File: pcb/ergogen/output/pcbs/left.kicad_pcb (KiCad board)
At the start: 2 copper layers, 143.4 x 86.2 mm, 49 parts

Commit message: Go Choc-only, add KiCad guide and case feel notes
- Drop the MX variant: one PCB per half with a Choc v1/v2 hot-swap
  footprint (center hole widened to 5.05mm for Choc v2).
- Ergogen outputs renamed to left/right PCBs and plate_left/right.
- docs/kicad-guide.md: beginner steps for finishing the PCB in KiCad.
- README: case ideas to keep a good typing feel (gasket mount,
  swappable plate materials, foam, flex cuts, weight).

Co-Authored-By: Claude Opus 5.5 <noreply@anthropic.com>
Claude-Session: https://claude.ai/code/session_017zNm7dMSTHELcztuNr6aNy
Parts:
- removed J1: , header6
- added D23: , ComboDiode, F.Cu at (95.2, -52.2)
- added D24: , ComboDiode, F.Cu at (114.3, 5.00)
- added D25: , ComboDiode, F.Cu at (104.8, -9.85)
- added ROT1: , rotary_encoder, F.Cu at (104.8, -19.1)
- added S23: , Choc_V1V2_Hotswap, F.Cu at (95.2, -57.2)
- added S24: , Choc_V1V2_Hotswap, F.Cu at (114.3, 0.00)
- S1, S10, S11, S12, S13, S14, S15, S16, S17, S18, S19, S2, S20, S21, S22, S3, S4, S5, S6, S7, S8, S9: footprint MX -> Choc_V1V2_Hotswap
- moved JST1 295.3 mm to (9.53, -9.53)
- moved D19 241.1 mm to (76.2, -33.1)
- moved D20 241.1 mm to (76.2, -52.2)
- moved D3 241.1 mm to (0.00, -33.1)
- moved D4 241.1 mm to (0.00, -52.2)
- moved D7 241.1 mm to (19.1, -33.1)
- moved D8 241.1 mm to (19.1, -52.2)
- moved S19 241.1 mm to (76.2, -38.1)
- moved S20 241.1 mm to (76.2, -57.2)
- moved S3 241.1 mm to (0.00, -38.1)
- moved S4 241.1 mm to (0.00, -57.2)
- moved S7 241.1 mm to (19.1, -38.1)
- moved S8 241.1 mm to (19.1, -57.2)
- moved D11 241.1 mm to (38.1, -33.1)
- moved D12 241.1 mm to (38.1, -52.2)
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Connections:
- net right_c10_bottom renamed left_c2_top
- net right_c10_home renamed left_c3_thumb
- net right_c10_thumb renamed left_c2_home
- net right_c10_top renamed left_c3_bottom
- net right_c11_bottom renamed left_c3_top
- net right_c11_home renamed left_c4_thumb
- net right_c11_thumb renamed left_c3_home
- net right_c11_top renamed left_c4_bottom
- net right_c12_bottom renamed left_c4_top
- net right_c12_home renamed left_c5_thumb
- net right_c12_thumb renamed left_c4_home
- net right_c12_top renamed left_c5_home
- net right_c8_bottom renamed left_c0_top
- net right_c8_home renamed left_c1_thumb
- net right_c8_thumb renamed left_c0_home
- net right_c8_top renamed left_c1_bottom
- net right_c9_bottom renamed left_c1_top
- net right_c9_home renamed left_c2_thumb
- net right_c9_thumb renamed left_c1_home
- net right_c9_top renamed left_c2_bottom
- net right_e_home renamed left_c0_thumb
- net right_e_top renamed left_c0_bottom
- D1 pad 1: ROW1 -> ROW3
- D10 pad 1: ROW0 -> ROW2
- D11 pad 1: ROW3 -> ROW1
- D12 pad 1: ROW2 -> ROW0
- D13 pad 1: ROW1 -> ROW3
- D14 pad 1: ROW0 -> ROW2
- D15 pad 1: ROW3 -> ROW1
- D16 pad 1: ROW2 -> ROW0
- D17 pad 1: ROW1 -> ROW3
- D18 pad 1: ROW0 -> ROW2
- D19 pad 1: ROW3 -> ROW1
- D2 pad 1: ROW0 -> ROW2
- D20 pad 1: ROW2 -> ROW0
- D21 pad 1: ROW1 -> ROW3
- D22 pad 1: ROW0 -> ROW1
- D3 pad 1: ROW3 -> ROW1
- D4 pad 1: ROW2 -> ROW0
- D5 pad 1: ROW1 -> ROW3
- D6 pad 1: ROW0 -> ROW2
- D7 pad 1: ROW3 -> ROW1
- D8 pad 1: ROW2 -> ROW0
- D9 pad 1: ROW1 -> ROW3
- S1 pad 1: COL7 -> COL0
- S10 pad 1: COL9 -> COL2
- S11 pad 1: COL10 -> COL2
- S12 pad 1: COL10 -> COL2
- S13 pad 1: COL10 -> COL3
- S14 pad 1: COL10 -> COL3
- S15 pad 1: COL11 -> COL3
- S16 pad 1: COL11 -> COL3
- S17 pad 1: COL11 -> COL4
- S18 pad 1: COL11 -> COL4
- S19 pad 1: COL12 -> COL4
- S2 pad 1: COL7 -> COL0
- S20 pad 1: COL12 -> COL4
- S21 pad 1: COL12 -> COL5
- S22 pad 1: COL12 -> COL5
- S3 pad 1: COL8 -> COL0
- S4 pad 1: COL8 -> COL0
- S5 pad 1: COL8 -> COL1
- S6 pad 1: COL8 -> COL1
- S7 pad 1: COL9 -> COL1
- S8 pad 1: COL9 -> COL1
- S9 pad 1: COL9 -> COL2
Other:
- board size 143.4 x 86.2 mm -> 143.3 x 86.2 mm

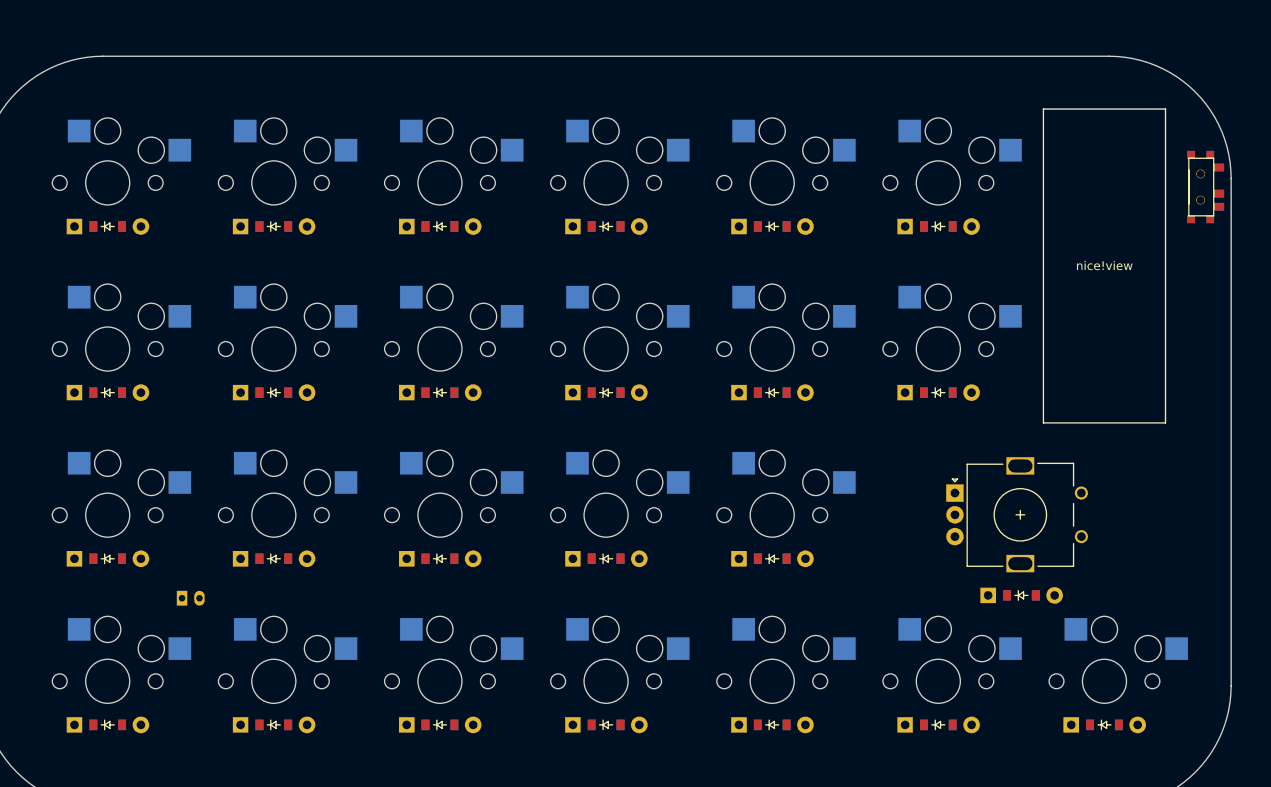
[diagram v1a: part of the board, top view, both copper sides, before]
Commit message: Use Choc v2 and ceoloide footprints for switches and peripherals
- Switches: ceoloide switch_choc_v1_v2 with v2 only (5.0mm center hole),
  hot-swap sockets on the back.
- nice!view, EC11 encoder, side power switch (Alps SSSS811101) and
  JST PH battery connector now use ceoloide footprints; nice!view is
  rotated so its pins face the XIAO and USB-C.
- Vendored footprints keep their licenses; README notes that the
  CC-BY-NC-SA parts block selling boards built from them.
- Only the XIAO nRF52840 Plus remains a placeholder.

Co-Authored-By: Claude Opus 5.5 <noreply@anthropic.com>
Claude-Session: https://claude.ai/code/session_017zNm7dMSTHELcztuNr6aNy
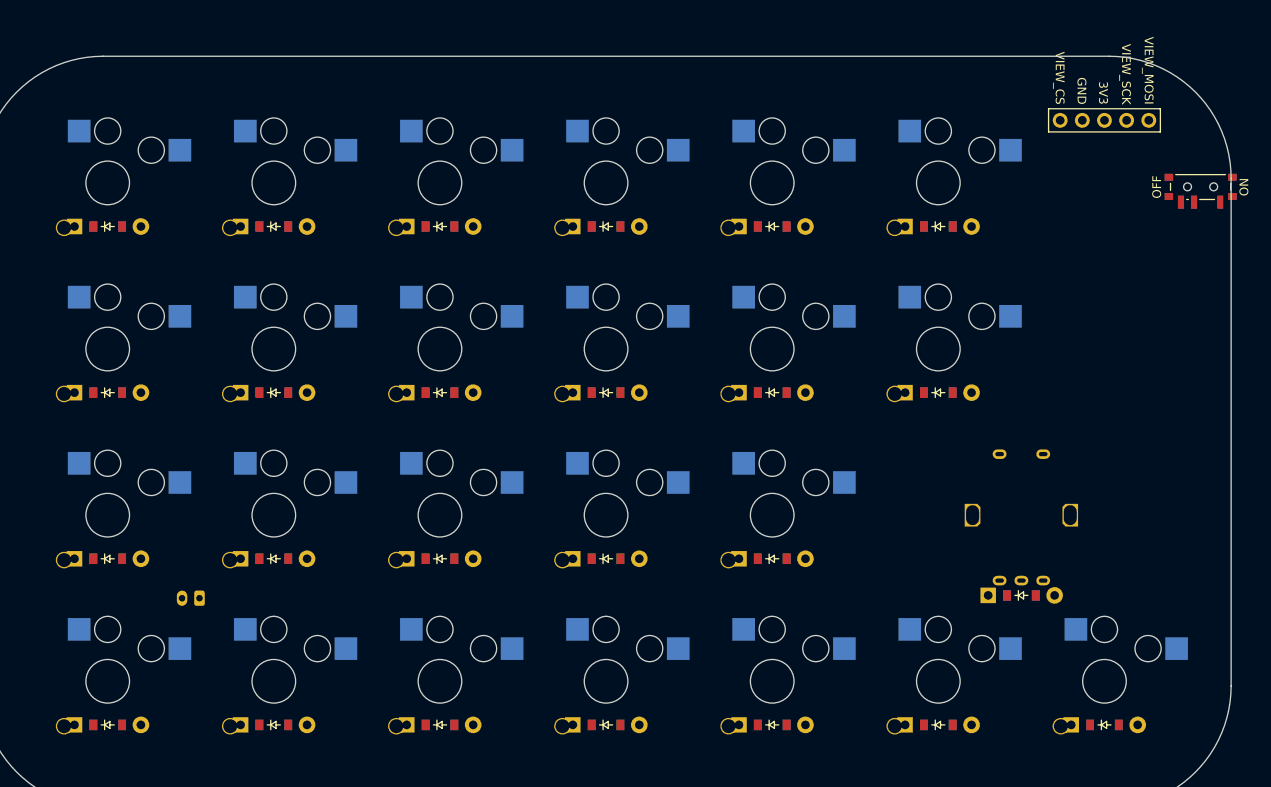
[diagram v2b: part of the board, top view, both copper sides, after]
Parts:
- removed BOX2: , box
- removed ROT1: , rotary_encoder
- removed T1: , E73:SPDT_C128955
- added DISP1: , ceoloide:display_nice_view, F.Cu at (114.3, -47.6)
- added PWR1: , ceoloide:power_switch_smd_side, F.Cu at (125.3, -56.7)
- added RE1: , ceoloide:rotary_encoder_ec11_ec12, F.Cu at (104.8, -19.1)
- JST1: footprint JST_PH_S2B-PH-K_02x2.00mm_Angled -> ceoloide:battery_connector_jst_ph_2; moved to B.Cu
- S1, S10, S11, S12, S13, S14, S15, S16, S17, S18, S19, S2, S20, S21, S22, S23, S24, S3, S4, S5, S6, S7, S8, S9: footprint Choc_V1V2_Hotswap -> ceoloide:switch_choc_v1_v2; moved to B.Cu
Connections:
- JST1 pad 1: BAT_P -> GND
- JST1 pad 2: GND -> BAT_P

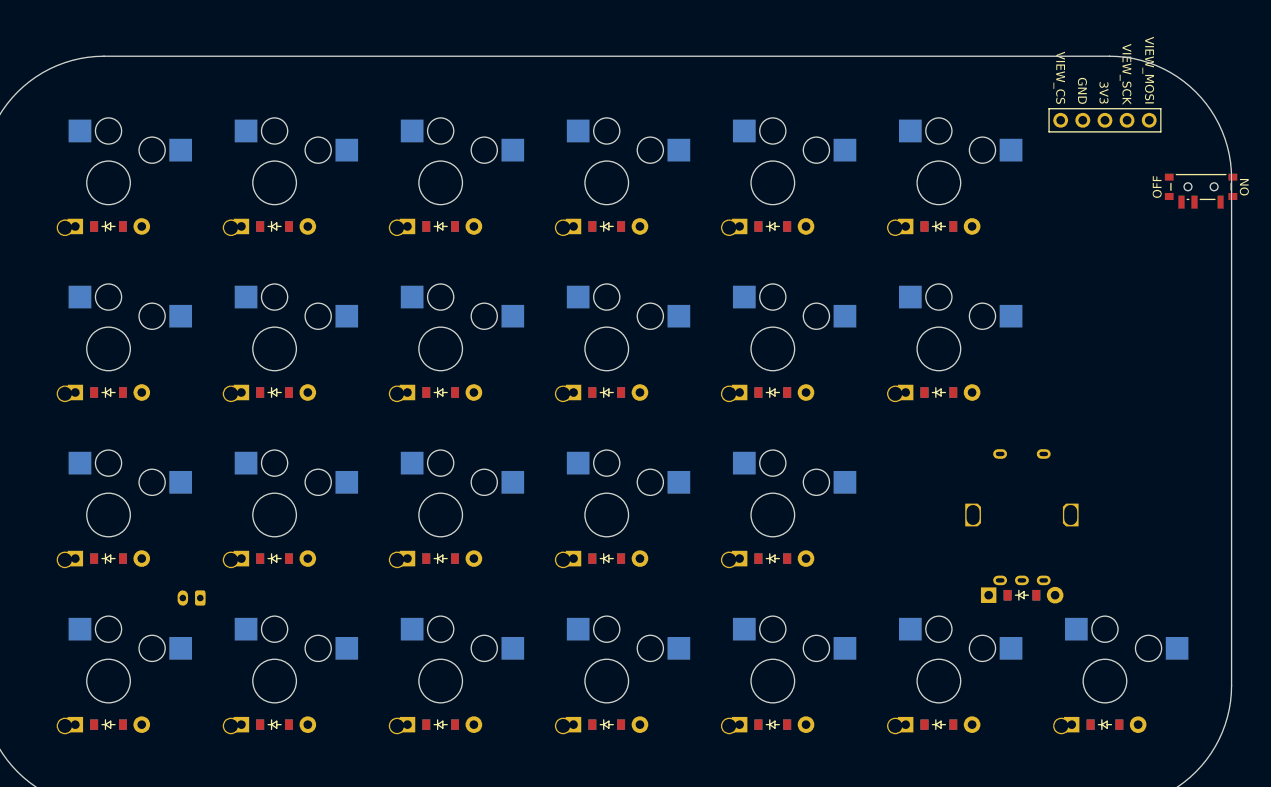
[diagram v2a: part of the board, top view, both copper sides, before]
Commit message: Replace non-commercial footprints with own ones so the PCB can be sold
- New kataware footprints: Choc v2 hot-swap (derived from Ergogen's MIT
  choc footprint, 5.0mm center hole, corner leg hole), nice!view (5 pins
  + outline), power switch placeholder (swap to KiCad SW_SPDT_PCM12) and
  an XIAO nRF52840 Plus placeholder carrying every pin's net per the
  firmware pin map.
- Keep only MIT ceoloide footprints (encoder, JST PH); drop the
  CC-BY-NC-SA ones.
- README and KiCad guide: license table and placeholder replacement.

Co-Authored-By: Claude Opus 5.5 <noreply@anthropic.com>
Claude-Session: https://claude.ai/code/session_017zNm7dMSTHELcztuNr6aNy
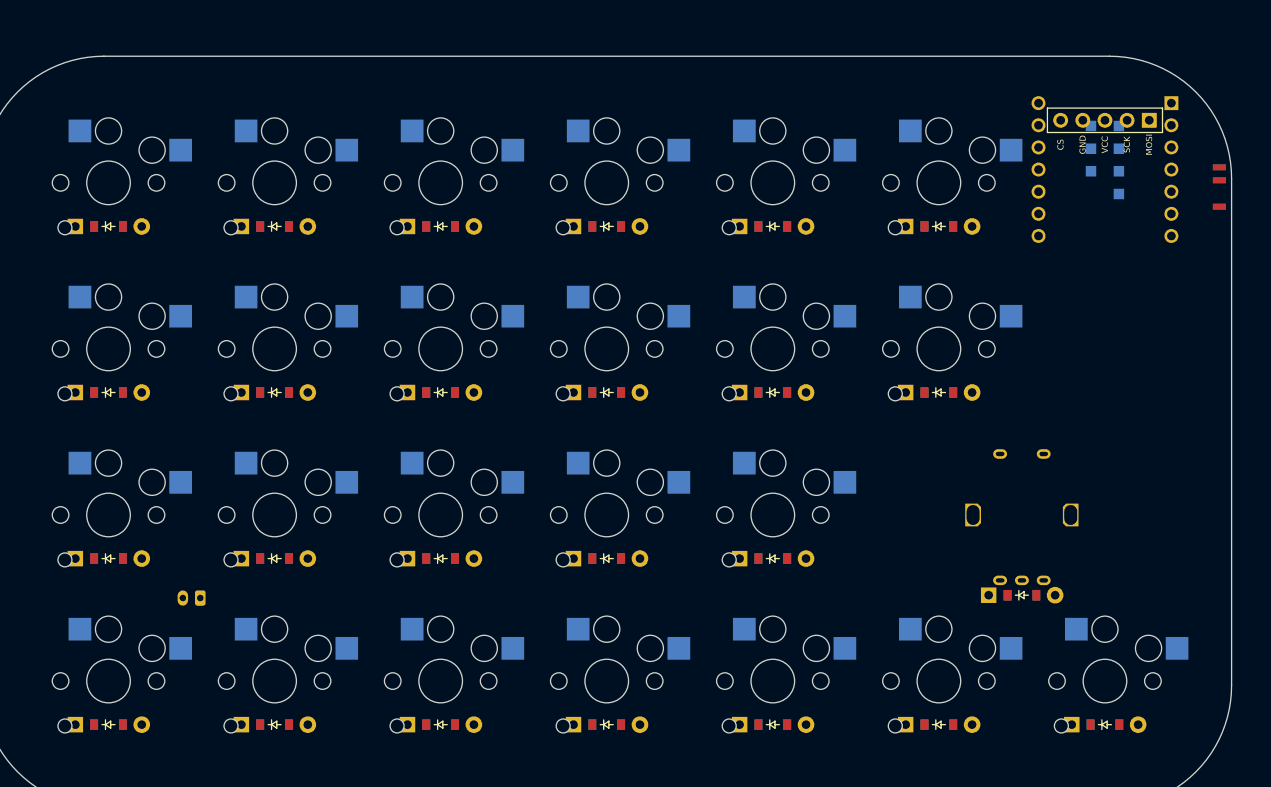
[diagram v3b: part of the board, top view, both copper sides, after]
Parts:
- removed BOX1: , box
- added MCU1: , kataware_xiao_plus_placeholder, B.Cu at (114.3, -58.7)
- DISP1: footprint ceoloide:display_nice_view -> kataware_nice_view
- PWR1: footprint ceoloide:power_switch_smd_side -> kataware_power_switch_placeholder
- S1, S10, S11, S12, S13, S14, S15, S16, S17, S18, S19, S2, S20, S21, S22, S23, S24, S3, S4, S5, S6, S7, S8, S9: footprint ceoloide:switch_choc_v1_v2 -> kataware_choc_v2_hotswap; moved to F.Cu

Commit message: Use a 1.25mm battery connector placeholder for the Gexa GA-011
The Gexa battery has a white 2-pin 1.25mm connector with no latch
(likely Molex PicoBlade compatible); viewed from the terminal face,
left is black (-) and right is red (+). The placeholder has pad 1 = GND
and pad 2 = BAT_P and is to be swapped for KiCad's PicoBlade footprint,
with polarity checked against the real battery.

Co-Authored-By: Claude Opus 5.5 <noreply@anthropic.com>
Claude-Session: https://claude.ai/code/session_017zNm7dMSTHELcztuNr6aNy
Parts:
- removed JST1: , ceoloide:battery_connector_jst_ph_2
- added BAT1: , kataware_battery_125_placeholder, B.Cu at (9.53, -9.53)
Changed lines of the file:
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@@
 (net 44 "BAT_SW")
 (net 45 "BAT_P")
-(net 46 "JST1_1")
-(net 47 "JST1_2")
     (module kataware_choc_v2_hotswap (layer F.Cu)
     (at 0 0 0)
@@
     (pad 3 smd rect (at 2.25 2.1 90) (size 0.7 1.5) (layers F.Cu F.Paste F.Mask))
     )
-    (footprint "ceoloide:battery_connector_jst_ph_2"
-        (layer "B.Cu")
-        (at 9.525 -9.525 0)
-        (property "Reference" "JST1"
-            (at 0 4.8 0)
-            (layer "B.SilkS")
-            hide
-            (effects (font (size 1 1) (thickness 0.15)))
-        )
-        (fp_line (start -2.95 -1.35) (end -2.25 -1.35) (stroke (width 0.1) (type solid)) (layer "B.Fab"))
-        (fp_line (start -2.95 6.25) (end -2.95 -1.35) (stroke (width 0.1) (type solid)) (layer "B.Fab"))
-        (fp_line (start -2.25 -1.35) (end -2.25 0.25) (stroke (width 0.1) (type solid)) (layer "B.Fab"))
-        (fp_line (start -2.25 0.25) (end 2.25 0.25) (stroke (width 0.1) (type solid)) (layer "B.Fab"))
-        (fp_line (start 2.25 -1.35) (end 2.95 -1.35) (stroke (width 0.1) (type solid)) (layer "B.Fab"))
-        (fp_line (start 2.25 0.25) (end 2.25 -1.35) (stroke (width 0.1) (type solid)) (layer "B.Fab"))
-        (fp_line (start 2.95 -1.35) (end 2.95 6.25) (stroke (width 0.1) (type solid)) (layer "B.Fab"))
-        (fp_line (start 2.95 6.25) (end -2.95 6.25) (stroke (width 0.1) (type solid)) (layer "B.Fab"))
-        (fp_line (start -3.45 -1.85) (end -3.45 10.5) (stroke (width 0.05) (type solid)) (layer "B.CrtYd"))
-        (fp_line (start -3.45 10.5) (end 3.45 10.5) (stroke (width 0.05) (type solid)) (layer "B.CrtYd"))
-        (fp_line (start 3.45 -1.85) (end -3.45 -1.85) (stroke (width 0.05) (type solid)) (layer "B.CrtYd"))
-        (fp_line (start 3.45 10.5) (end 3.45 -1.85) (stroke (width 0.05) (type solid)) (layer "B.CrtYd"))
-        (fp_line (start 1.5 7.40) (end 0.5 7.40) (stroke (width 0.1) (type solid)) (layer "B.SilkS"))
-        (fp_line (start -1.5 7.40) (end -0.5 7.40) (stroke (width 0.1) (type solid)) (layer "B.SilkS"))
-        (fp_line (start -1 6.90) (end -1 7.90) (stroke (width 0.1) (type solid)) (layer "B.SilkS"))
-        (fp_line (start -2.06 -1.46) (end -3.06 -1.46) (stroke (width 0.12) (type solid)) (layer "B.SilkS"))
-        (fp_line (start -3.06 -1.46) (end -3.06 -0.46) (stroke (width 0.12) (type solid)) (layer "B.SilkS"))
-        (fp_line (start 2.14 -1.46) (end 3.06 -1.46) (stroke (width 0.12) (type solid)) (layer "B.SilkS"))
-        (fp_line (start 3.06 -1.46) (end 3.06 -0.46) (stroke (width 0.12) (type solid)) (layer "B.SilkS"))
-        (fp_line (start -2.14 6.36) (end -3.06 6.36) (stroke (width 0.12) (type solid)) (layer "B.SilkS"))
-        (fp_line (start -3.06 6.36) (end -3.06 5.36) (stroke (width 0.12) (type solid)) (layer "B.SilkS"))
-        (fp_line (start 2.14 6.36) (end 3.06 6.36) (stroke (width 0.12) (type solid)) (layer "B.SilkS"))
-        (fp_line (start 3.06 6.36) (end 3.06 5.36) (stroke (width 0.12) (type solid)) (layer "B.SilkS"))
-        (pad "1" thru_hole roundrect (at 1 0 0) (size 1.2 1.75) (drill 0.75) (layers "*.Cu" "*.Mask") (roundrect_rratio 0.20) (net 38 "GND"))
-        (pad "2" thru_hole oval (at -1 0 0) (size 1.2 1.75) (drill 0.75) (layers "*.Cu" "*.Mask") (net 45 "BAT_P"))
+    (module kataware_battery_125_placeholder (layer B.Cu)
+    (at 9.525 -9.525 0)
+    (fp_text reference "BAT1" (at 0 -3) (layer B.SilkS) hide (effects (font (size 1 1) (thickness 0.15)) (justify mirror)))
+    (fp_text value "" (at 0 0) (layer B.SilkS) hide (effects (font (size 1 1) (thickness 0.15)) (justify mirror)))
+    (fp_text user "BAT 1.25mm (仮)" (at 0 3 0) (layer B.Fab) (effects (font (size 0.8 0.8) (thickness 0.12)) (justify mirror)))
+    (fp_text user "-" (at -0.625 -1.8 0) (layer B.SilkS) (effects (font (size 1 1) (thickness 0.15)) (justify mirror)))
+    (fp_text user "+" (at 0.625 -1.8 0) (layer B.SilkS) (effects (font (size 1 1) (thickness 0.15)) (justify mirror)))
+    (fp_line (start -2.5 -1) (end 2.5 -1) (layer B.Fab) (width 0.12))
+    (fp_line (start 2.5 -1) (end 2.5 2.2) (layer B.Fab) (width 0.12))
+    (fp_line (start 2.5 2.2) (end -2.5 2.2) (layer B.Fab) (width 0.12))
+    (fp_line (start -2.5 2.2) (end -2.5 -1) (layer B.Fab) (width 0.12))
+    (pad 1 smd rect (at -0.625 0 0) (size 0.8 1.6) (layers B.Cu B.Paste B.Mask) (net 38 "GND"))
+    (pad 2 smd rect (at 0.625 0 0) (size 0.8 1.6) (layers B.Cu B.Paste B.Mask) (net 45 "BAT_P"))
     )
   (gr_line (start -0.5249999999999986 14.525000000000002) (end 114.82499999999999 14.525000000000002) (layer Edge.Cuts) (stroke (width 0.15) (type default)))
